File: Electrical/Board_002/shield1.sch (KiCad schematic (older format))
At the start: 8 parts, among them P1 Power, P2 Analog, P3 Digital, P4 Digital, P5 CONN_01X01, P6 CONN_01X01, P7 CONN_01X01, P8 CONN_01X01

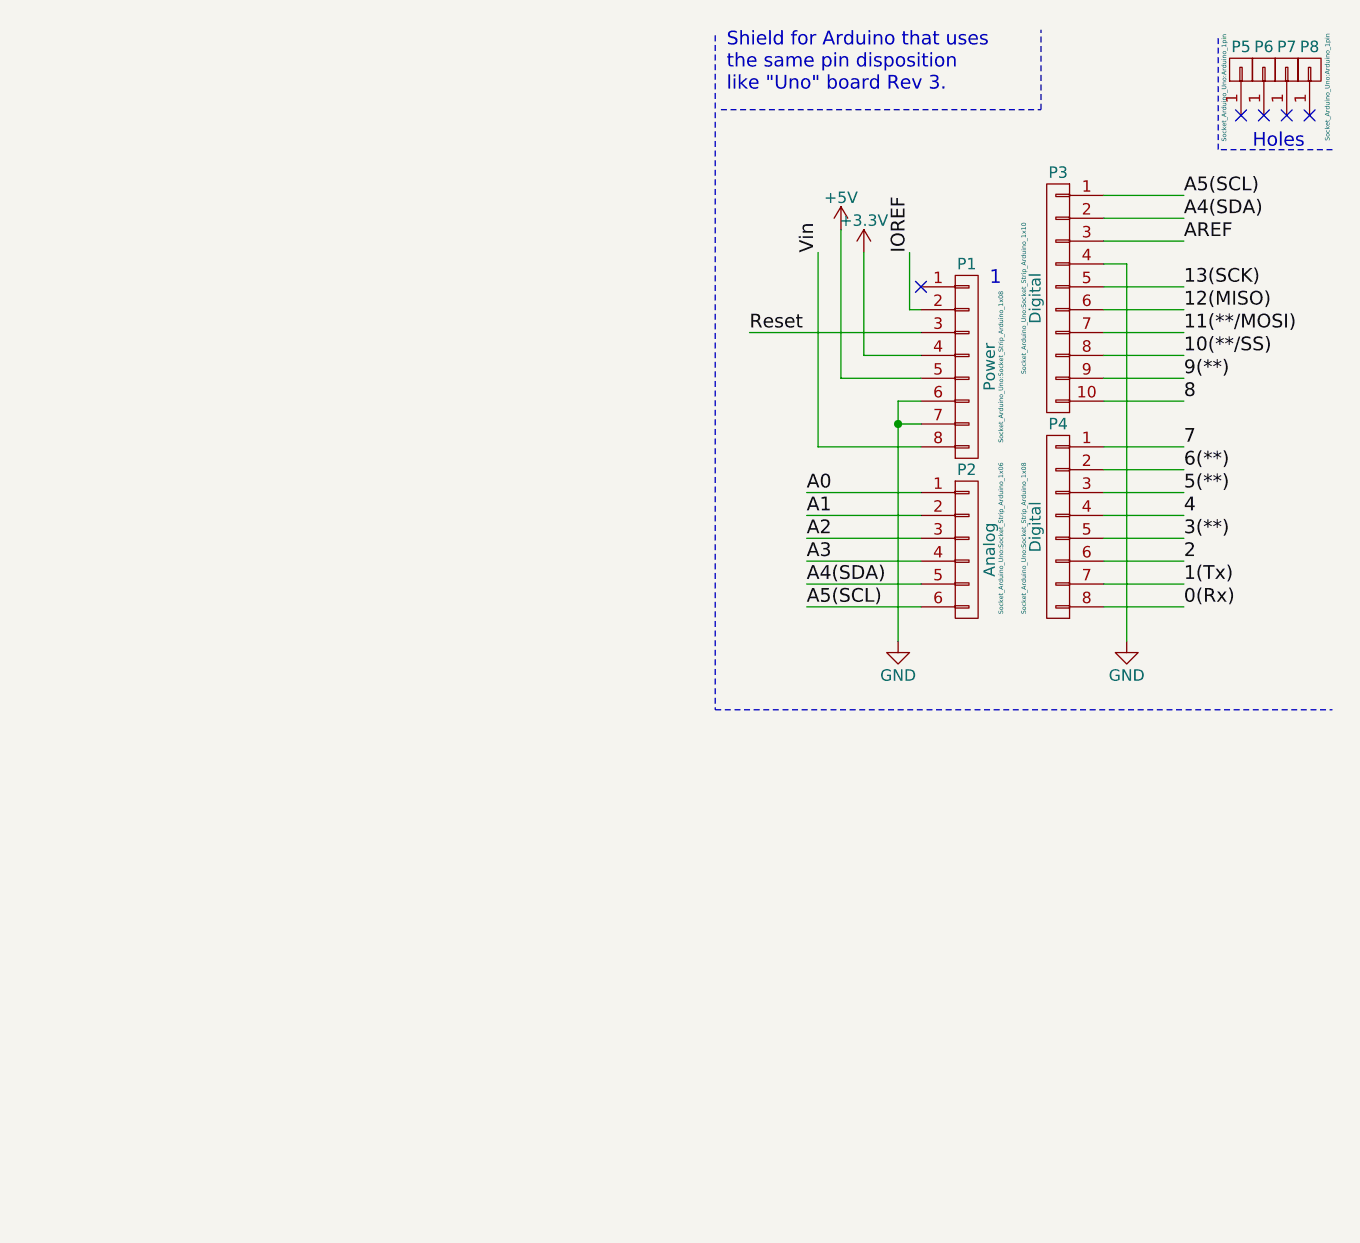
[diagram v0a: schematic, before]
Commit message: Board_002: Added TSS721 component - unfinished, not all pins configured correctly!
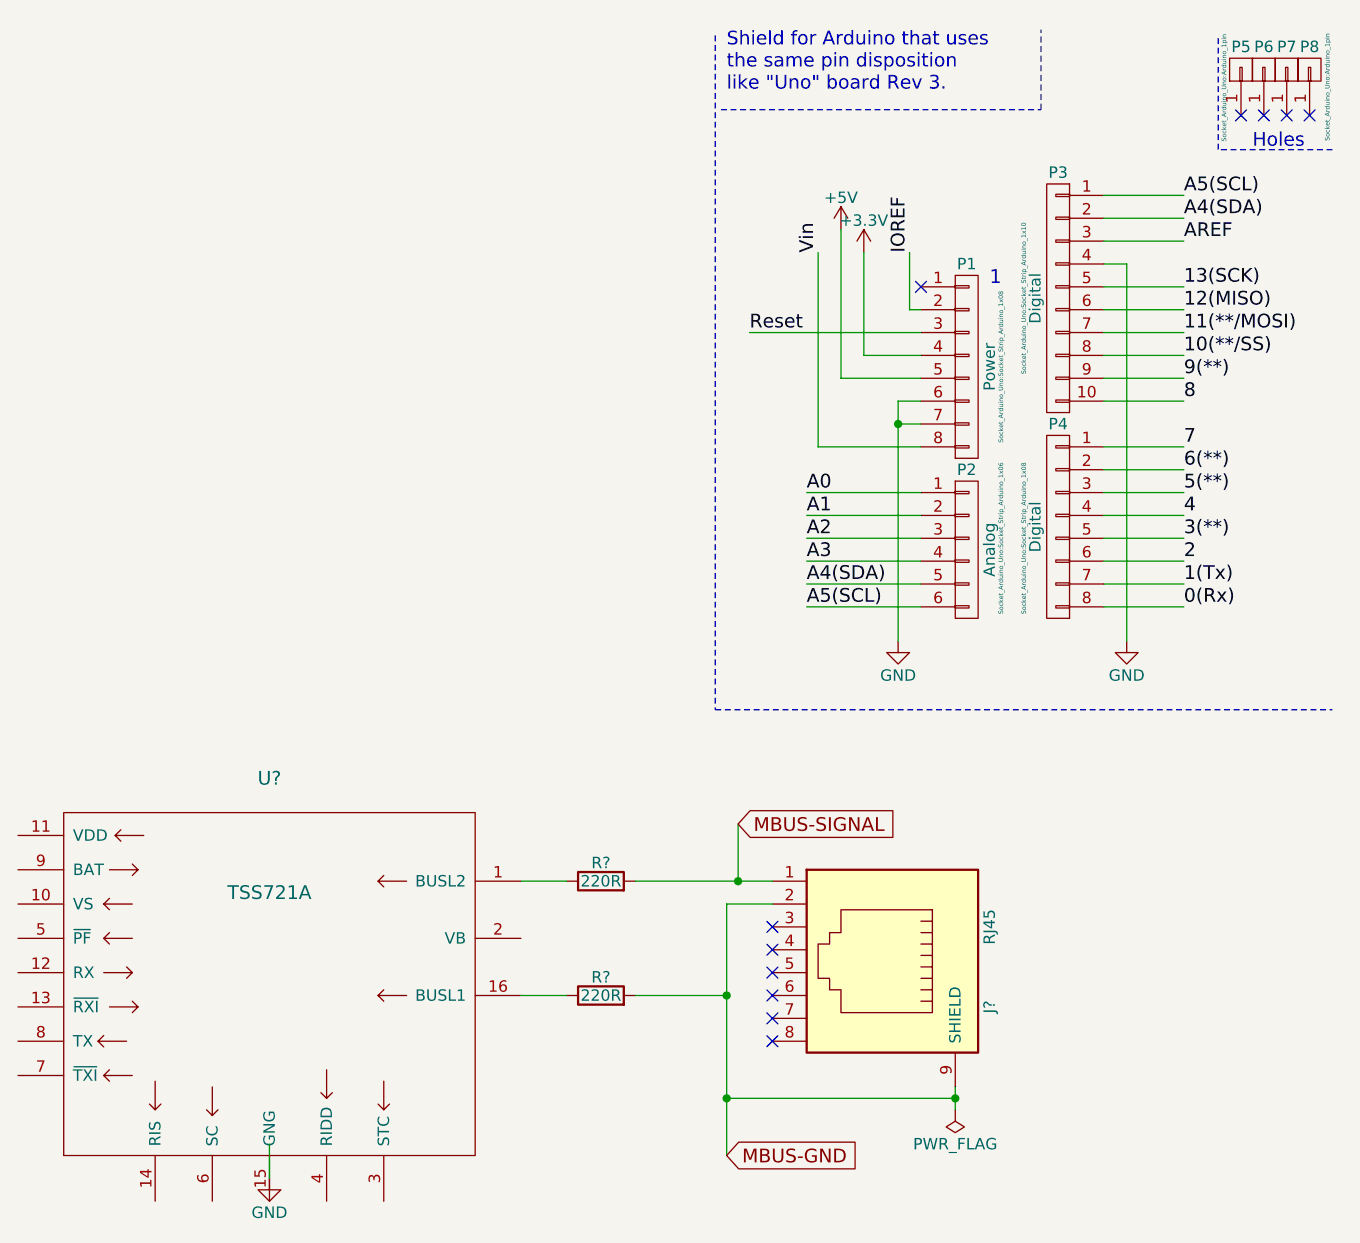
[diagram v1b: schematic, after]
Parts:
- added J?: RJ45, symbol RJ45
- added R? (x2): 220R, symbol R
- added U?: TSS721A, symbol TSS721A
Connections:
- new net: R?.1, U?.16 (BUSL1)
- new net: R?.1, U?.1 (BUSL2)
- new net MBUS-GND: J?.2, J?.9 (SHIELD), R?.2
- new net MBUS-SIGNAL: J?.1, R?.2
- no-connect marks 5 -> 11
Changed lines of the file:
@@
 LIBS:contrib
 LIBS:valves
-LIBS:Arduino_As_Uno-cache
+LIBS:amstomqtt
+LIBS:shield1-cache
 EELAYER 25 0
 EELAYER END
@@
 	10300 1500 10300 3150
 Wire Wire Line
-	9300 2100 9300 2200
-Wire Wire Line
-	9300 2200 9300 3150
+	9300 2100 9300 3150
 Wire Notes Line
 	8500 500  8500 3450
@@
 Wire Notes Line
 	10700 1000 10700 500
+$Comp
+L RJ45 J?
+U 1 1 5A5E7E25
+P 9200 4550
+F 0 "J?" H 9400 5050 50  0000 C CNN
+F 1 "RJ45" H 9050 5050 50  0000 C CNN
+F 2 "" H 9200 4550 50  0001 C CNN
+F 3 "" H 9200 4550 50  0001 C CNN
+	1    9200 4550
+	0    1    1    0
+$EndComp
+NoConn ~ 8750 4900
+NoConn ~ 8750 4800
+NoConn ~ 8750 4700
+NoConn ~ 8750 4600
+NoConn ~ 8750 4500
+NoConn ~ 8750 4400
+Text GLabel 8600 3950 2    60   Input ~ 0
+MBUS-SIGNAL
+Text GLabel 8550 5400 2    60   Input ~ 0
+MBUS-GND
+Wire Wire Line
+	8150 4200 8750 4200
+Wire Wire Line
+	8600 3950 8600 4200
+$Comp
+L PWR_FLAG #FLG?
+U 1 1 5A5E8423
+P 9550 5200
+F 0 "#FLG?" H 9550 5275 50  0001 C CNN
+F 1 "PWR_FLAG" H 9550 5350 50  0000 C CNN
+F 2 "" H 9550 5200 50  0001 C CNN
+F 3 "" H 9550 5200 50  0001 C CNN
+	1    9550 5200
+	-1   0    0    1
+$EndComp
+$Comp
+L R R?
+U 1 1 5A5E85D8
+P 8000 4700
+F 0 "R?" V 8080 4700 50  0000 C CNN
+F 1 "220R" V 8000 4700 50  0000 C CNN
+F 2 "" V 7930 4700 50  0001 C CNN
+F 3 "" H 8000 4700 50  0001 C CNN
+	1    8000 4700
+	0    -1   -1   0
+$EndComp
+Wire Wire Line
+	8750 4300 8550 4300
+$Comp
+L R R?
+U 1 1 5A5E86FE
+P 8000 4200
+F 0 "R?" V 8080 4200 50  0000 C CNN
+F 1 "220R" V 8000 4200 50  0000 C CNN
+F 2 "" V 7930 4200 50  0001 C CNN
+F 3 "" H 8000 4200 50  0001 C CNN
+	1    8000 4200
+	0    -1   -1   0
+$EndComp
+Wire Wire Line
+	9550 5100 9550 5200
+Wire Wire Line
+	8550 4300 8550 5400
+Wire Wire Line
+	9550 5150 8550 5150
+Connection ~ 9550 5150
+$Comp
+L TSS721A U?
+U 1 1 5A5E92ED
+P 6550 4550
+F 0 "U?" H 6550 5350 60  0000 C CNN
+F 1 "TSS721A" H 6550 4850 60  0000 C CNN
+F 2 "" H 6700 3700 60  0001 C CNN
+F 3 "" H 6700 3700 60  0001 C CNN
+	1    6550 4550
+	1    0    0    -1
+$EndComp
+Connection ~ 8550 5150
+Wire Wire Line
+	7650 4200 7850 4200
+Wire Wire Line
+	7650 4700 7850 4700
+Connection ~ 8600 4200
+Wire Wire Line
+	8150 4700 8550 4700
+Connection ~ 8550 4700
+$Comp
+L GND #PWR?
+U 1 1 5A5E9F25
+P 6550 5500
+F 0 "#PWR?" H 6550 5250 50  0001 C CNN
+F 1 "GND" H 6550 5350 50  0000 C CNN
+F 2 "" H 6550 5500 50  0001 C CNN
+F 3 "" H 6550 5500 50  0001 C CNN
+	1    6550 5500
+	1    0    0    -1
+$EndComp
+Wire Wire Line
+	6550 5350 6550 5500
 $EndSCHEMATC
